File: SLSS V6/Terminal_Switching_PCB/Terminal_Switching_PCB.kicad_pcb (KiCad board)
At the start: 2 copper layers, 58 x 48 mm, 4 parts, among them J1 +5V, J2 GND, J3 LED, J4 Solenoid

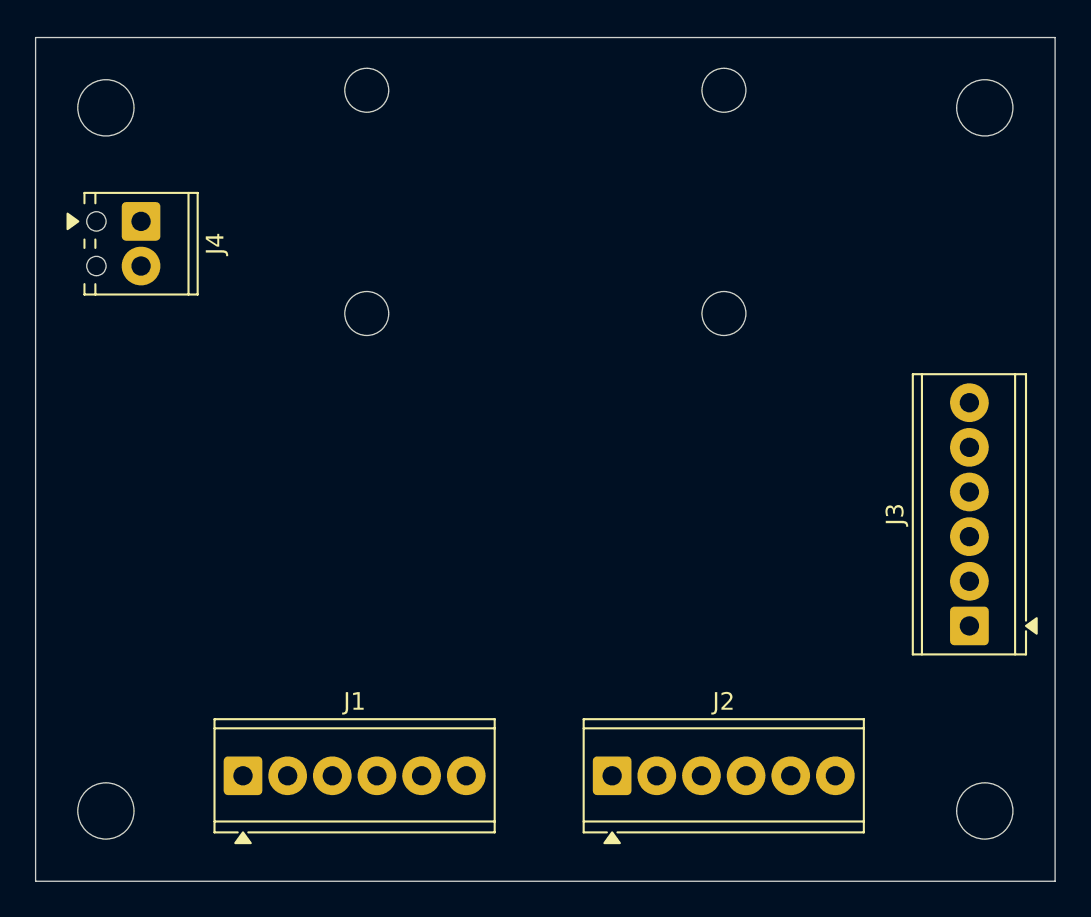
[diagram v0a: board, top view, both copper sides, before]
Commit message: Created first PCB
needs placement adjustment
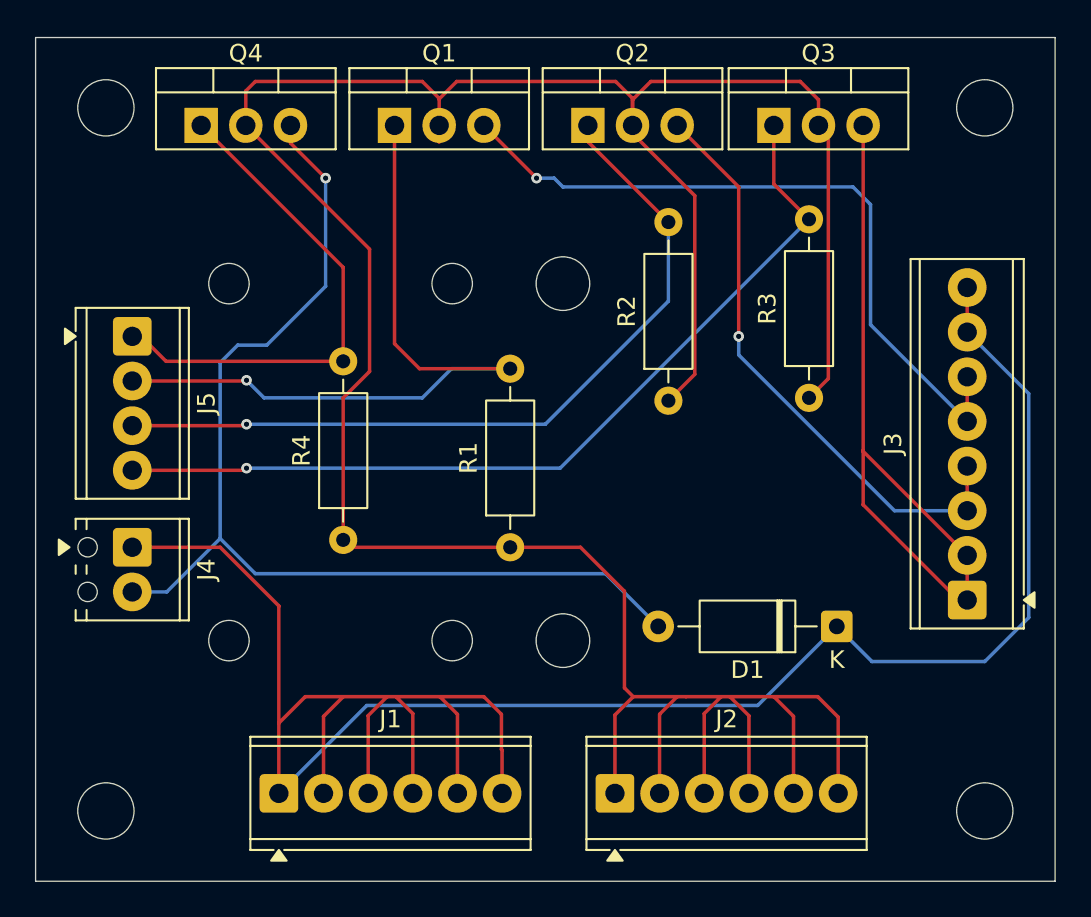
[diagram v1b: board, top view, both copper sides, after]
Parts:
- added D1: D, Diode_THT:D_A-405_P10.16mm_Horizontal, F.Cu at (148.6, 103.0)
- added J5: Arduino Pins, TerminalBlock_Phoenix:TerminalBlock_Phoenix_MPT-0,5-4-2.54_1x04_P2.54mm_Horizontal, F.Cu at (108.5, 86.5)
- added Q1: IRLZ34N, Package_TO_SOT_THT:TO-220-3_Vertical, F.Cu at (123.4, 74.5)
- added Q2: IRLZ34N, Package_TO_SOT_THT:TO-220-3_Vertical, F.Cu at (134.4, 74.5)
- added Q3: IRLZ34N, Package_TO_SOT_THT:TO-220-3_Vertical, F.Cu at (145.0, 74.5)
- added Q4: IRLZ34N, Package_TO_SOT_THT:TO-220-3_Vertical, F.Cu at (112.4, 74.5)
- added R1: 10k, Resistor_THT:R_Axial_DIN0207_L6.3mm_D2.5mm_P10.16mm_Horizontal, F.Cu at (130.0, 98.5)
- added R2: 10k, Resistor_THT:R_Axial_DIN0207_L6.3mm_D2.5mm_P10.16mm_Horizontal, F.Cu at (139.0, 90.2)
- added R3: 10k, Resistor_THT:R_Axial_DIN0207_L6.3mm_D2.5mm_P10.16mm_Horizontal, F.Cu at (147.0, 90.0)
- added R4: 10k, Resistor_THT:R_Axial_DIN0207_L6.3mm_D2.5mm_P10.16mm_Horizontal, F.Cu at (120.5, 98.1)
- J3: value LED -> RBG_LED_PINS; footprint TerminalBlock_Phoenix:TerminalBlock_Phoenix_MPT-0,5-6-2.54_1x06_P2.54mm_Horizontal -> TerminalBlock_Phoenix:TerminalBlock_Phoenix_MPT-0,5-8-2.54_1x08_P2.54mm_Horizontal
- moved J4 18.5 mm to (108.5, 98.5)
- moved J1 2.27 mm to (116.8, 112.5)
- moved J3 1.48 mm to (156.0, 101.5)
- moved J2 1.01 mm to (136.0, 112.5)
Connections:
- J1 pad 1: unconnected-(J1-Pin_1-Pad1) -> +5V OLED
- J1 pad 2: unconnected-(J1-Pin_2-Pad2) -> +5V OLED
- J1 pad 3: unconnected-(J1-Pin_3-Pad3) -> +5V OLED
- J1 pad 4: unconnected-(J1-Pin_4-Pad4) -> +5V OLED
- J1 pad 5: unconnected-(J1-Pin_5-Pad5) -> +5V OLED
- J1 pad 6: unconnected-(J1-Pin_6-Pad6) -> +5V OLED
- J2 pad 1: unconnected-(J2-Pin_1-Pad1) -> GND OLED
- J2 pad 2: unconnected-(J2-Pin_2-Pad2) -> GND OLED
- J2 pad 3: unconnected-(J2-Pin_3-Pad3) -> GND OLED
- J2 pad 4: unconnected-(J2-Pin_4-Pad4) -> GND OLED
- J2 pad 5: unconnected-(J2-Pin_5-Pad5) -> GND OLED
- J2 pad 6: unconnected-(J2-Pin_6-Pad6) -> GND OLED
- J3 pad 1: unconnected-(J3-Pin_1-Pad1) -> Net-(J3-Pin_1)
- J3 pad 2: unconnected-(J3-Pin_2-Pad2) -> Net-(J3-Pin_1)
- J3 pad 3: unconnected-(J3-Pin_3-Pad3) -> Net-(J3-Pin_3)
- J3 pad 4: unconnected-(J3-Pin_4-Pad4) -> Net-(J3-Pin_3)
- J3 pad 5: unconnected-(J3-Pin_5-Pad5) -> Net-(J3-Pin_5)
- J3 pad 6: unconnected-(J3-Pin_6-Pad6) -> Net-(J3-Pin_5)
- J4 pad 1: unconnected-(J4-Pin_1-Pad1) -> +5V OLED
- J4 pad 2: unconnected-(J4-Pin_2-Pad2) -> Net-(D1-A)
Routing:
- net GND OLED: track 0.00 -> 175.3 mm
- net +5V OLED: track 0.00 -> 131.0 mm
- net Net-(D1-A): track 0.00 -> 61.0 mm, vias 0 -> 1
- net Net-(J5-Pin_4): track 0.00 -> 50.6 mm, vias 0 -> 1
- net Net-(J5-Pin_3): track 0.00 -> 45.3 mm, vias 0 -> 1
- net Net-(J5-Pin_2): track 0.00 -> 42.2 mm, vias 0 -> 1
- net Net-(J3-Pin_5): track 0.00 -> 41.0 mm, vias 0 -> 1
- net Net-(J3-Pin_1): track 0.00 -> 40.7 mm
- net Net-(J3-Pin_3): track 0.00 -> 33.7 mm, vias 0 -> 1
- net Net-(J5-Pin_1): track 0.00 -> 29.4 mm
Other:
- outline, holes or cut-outs redrawn

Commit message: commit
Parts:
- moved D1 4.50 mm to (148.6, 98.5)
- moved R2 2.00 mm to (141.0, 90.1)
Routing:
- net GND OLED: track 175.3 -> 189.6 mm
- net +5V OLED: track 131.0 -> 135.5 mm
- net Net-(J5-Pin_3): track 45.3 -> 49.1 mm
- net Net-(D1-A): track 61.0 -> 62.7 mm
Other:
- outline, holes or cut-outs redrawn
